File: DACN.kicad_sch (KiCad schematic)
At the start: 0 parts

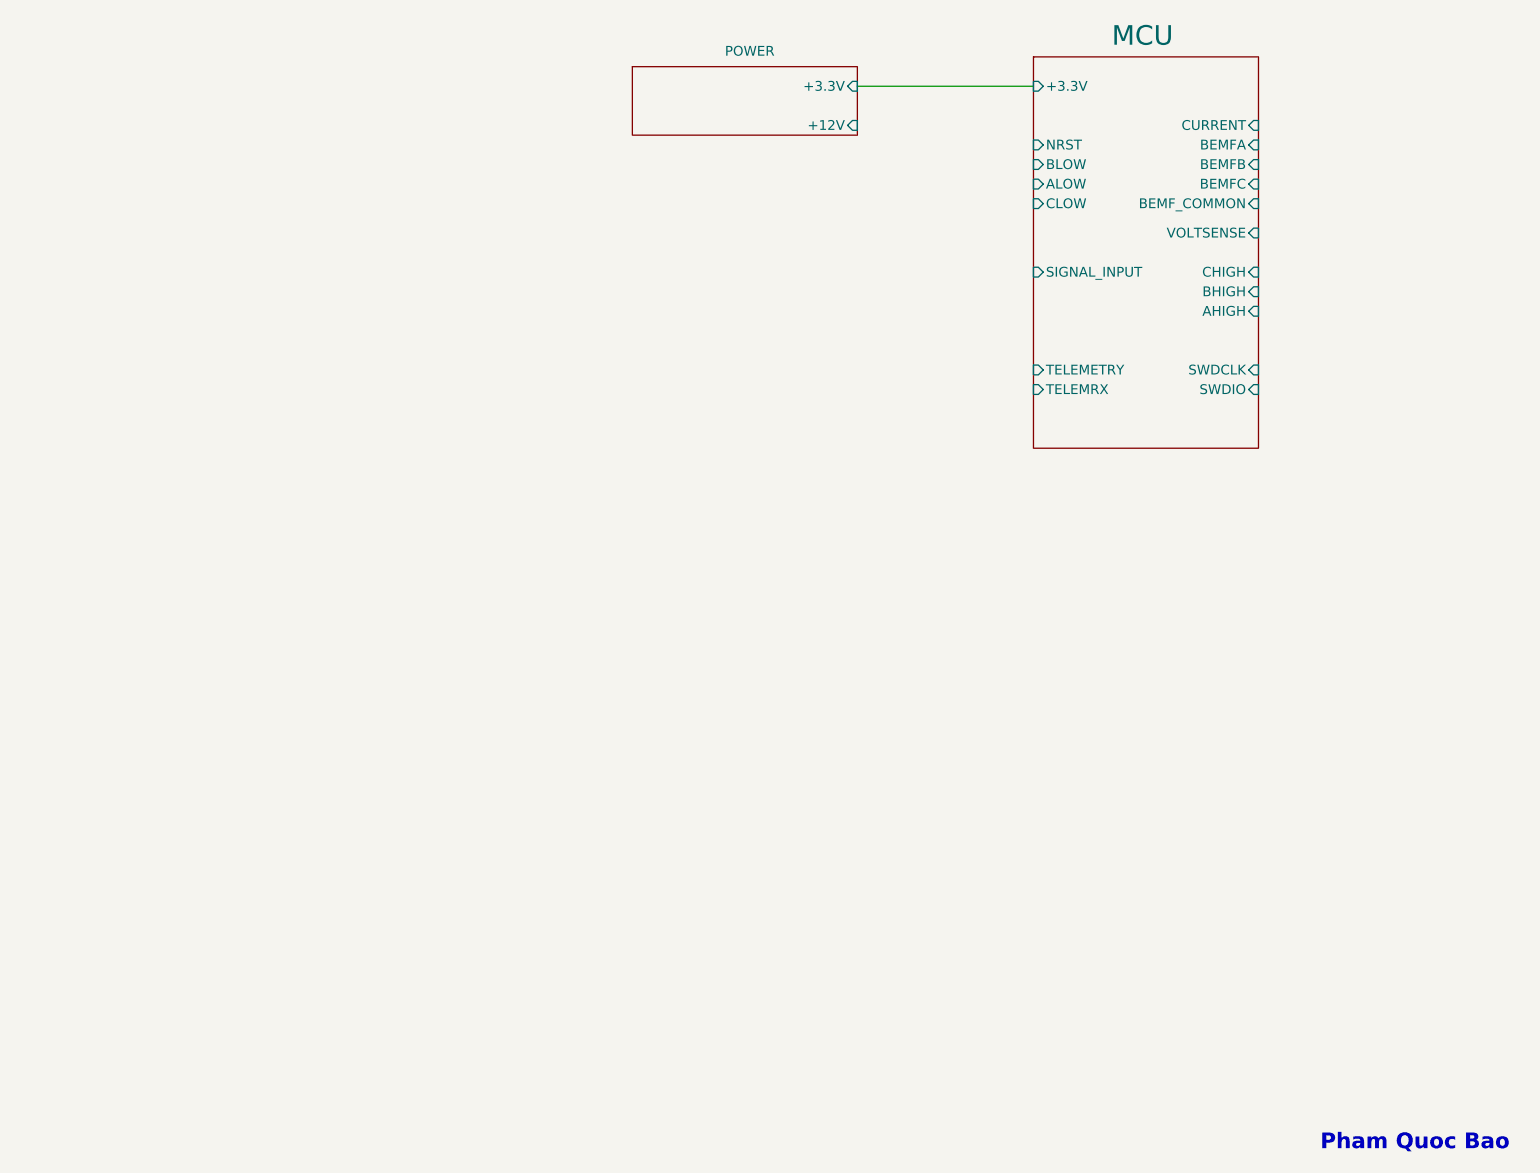
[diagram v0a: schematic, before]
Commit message: add driver and mosfet
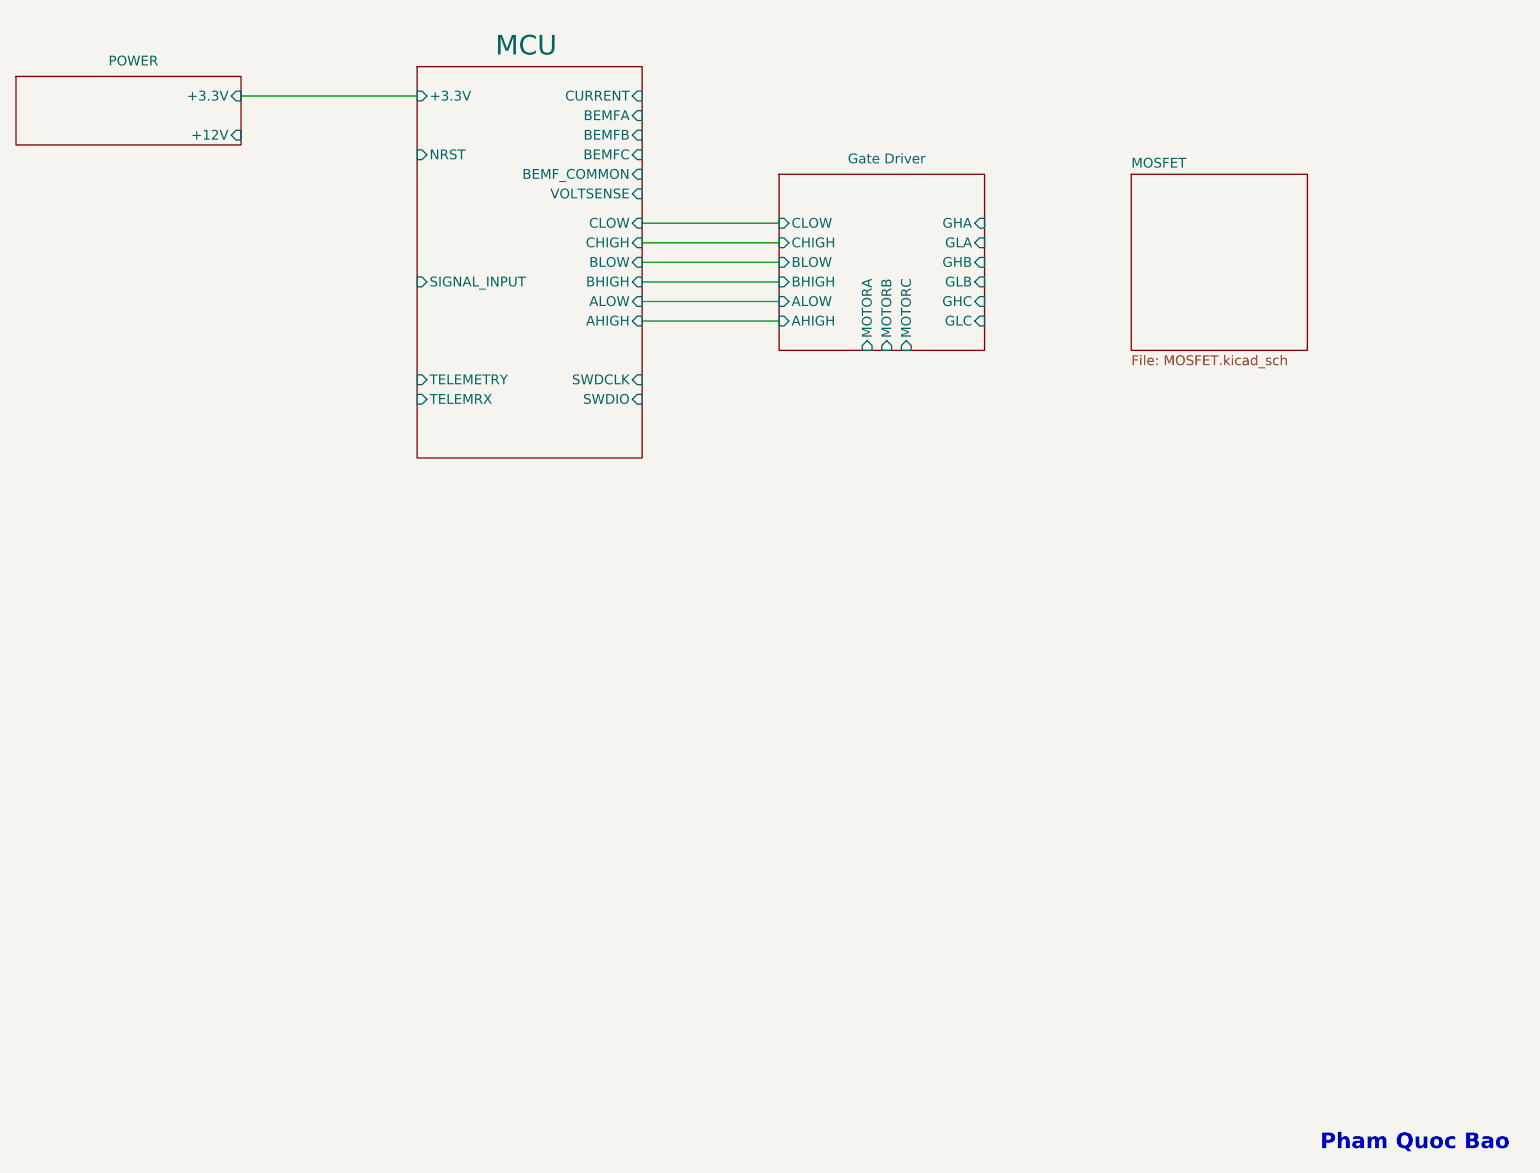
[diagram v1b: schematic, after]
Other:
- added sheet Gate Driver (Gate Driver.kicad_sch)
- added sheet MOSFET (MOSFET.kicad_sch)

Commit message: add
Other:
- sheet MOSFET ports: added CURRENT, GHA, GHB, GHC, GLA, GLB, GLC, MOTORA, MOTORB, MOTORC; removed none

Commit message: Add connectors,..
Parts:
- added C31: 100n, Capacitor_SMD:C_0603_1608Metric_Pad1.08x0.95mm_HandSolder, symbol PCM_SL_Devices:Capacitor_NP
- added D4: LED, LED_SMD:LED_0603_1608Metric, symbol PCM_SL_Devices:LED_3mm
- added H1, H2, H3, H4: MountingHole_M3_3.2mm_Pad, PCM_SL_Mechanical:MountingHole_3.2mm_Pad, symbol PCM_SL_Mechanical:MountingHole_M3_3.2mm_Pad
- added J1: PINHD_1x5_Male, Connector_PinHeader_2.54mm:PinHeader_1x05_P2.54mm_Vertical, symbol PCM_SL_Pin_Headers:PINHD_1x5_Male
- added R13, R14, R27: 100K, Resistor_THT:R_Axial_DIN0207_L6.3mm_D2.5mm_P10.16mm_Horizontal, symbol PCM_SL_Resistors:Resistor
- added R5: 1K5, Resistor_THT:R_Axial_DIN0207_L6.3mm_D2.5mm_P10.16mm_Horizontal, symbol PCM_SL_Resistors:Resistor
- added TP1, TP2, TP3, TP4, TP5, TP6, TP7, TP8, TP9: 0.5mm, PCM_SparkFun-Connector:TestPoint-0.5mm, symbol PCM_SparkFun-Connector:TestPoint_0.5mm
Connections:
- net MCU/NRST: now also TP3.1
- net MCU/SWDCLK: now also TP2.1
- net MCU/SWDIO: now also TP1.1
- net MCU/TELEMRX: now also TP6.1
- net MCU/VOLTSENSE: now also C31.2, R27.1
- new net: R13.1, R14.2, R27.2
- new net: D4.1, R5.2
- new net +3.3V: D4.2, TP4.1
- new net +BATT: J1.1, R13.2
- new net CURRENT: J1.3, TP7.1
- new net GND: C31.1, H1.1, H2.1, H3.1, H4.1, J1.2, R14.1, R5.1, TP5.1
- new net SIGNAL_INPUT: J1.4, TP8.1
- new net TELEMETRY: J1.5, TP9.1
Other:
- added sheet BEMF (BEMF.kicad_sch)
- sheet MCU ports: added none; removed +3.3V
- sheet POWER ports: added none; removed +12V, +3.3V
